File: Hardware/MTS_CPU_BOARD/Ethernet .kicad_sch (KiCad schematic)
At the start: 7 parts, among them J2 THD-02-R, U4 TPD4EUSB30, U5 TPD4EUSB30, U6 MagJack-A70-112-331N126

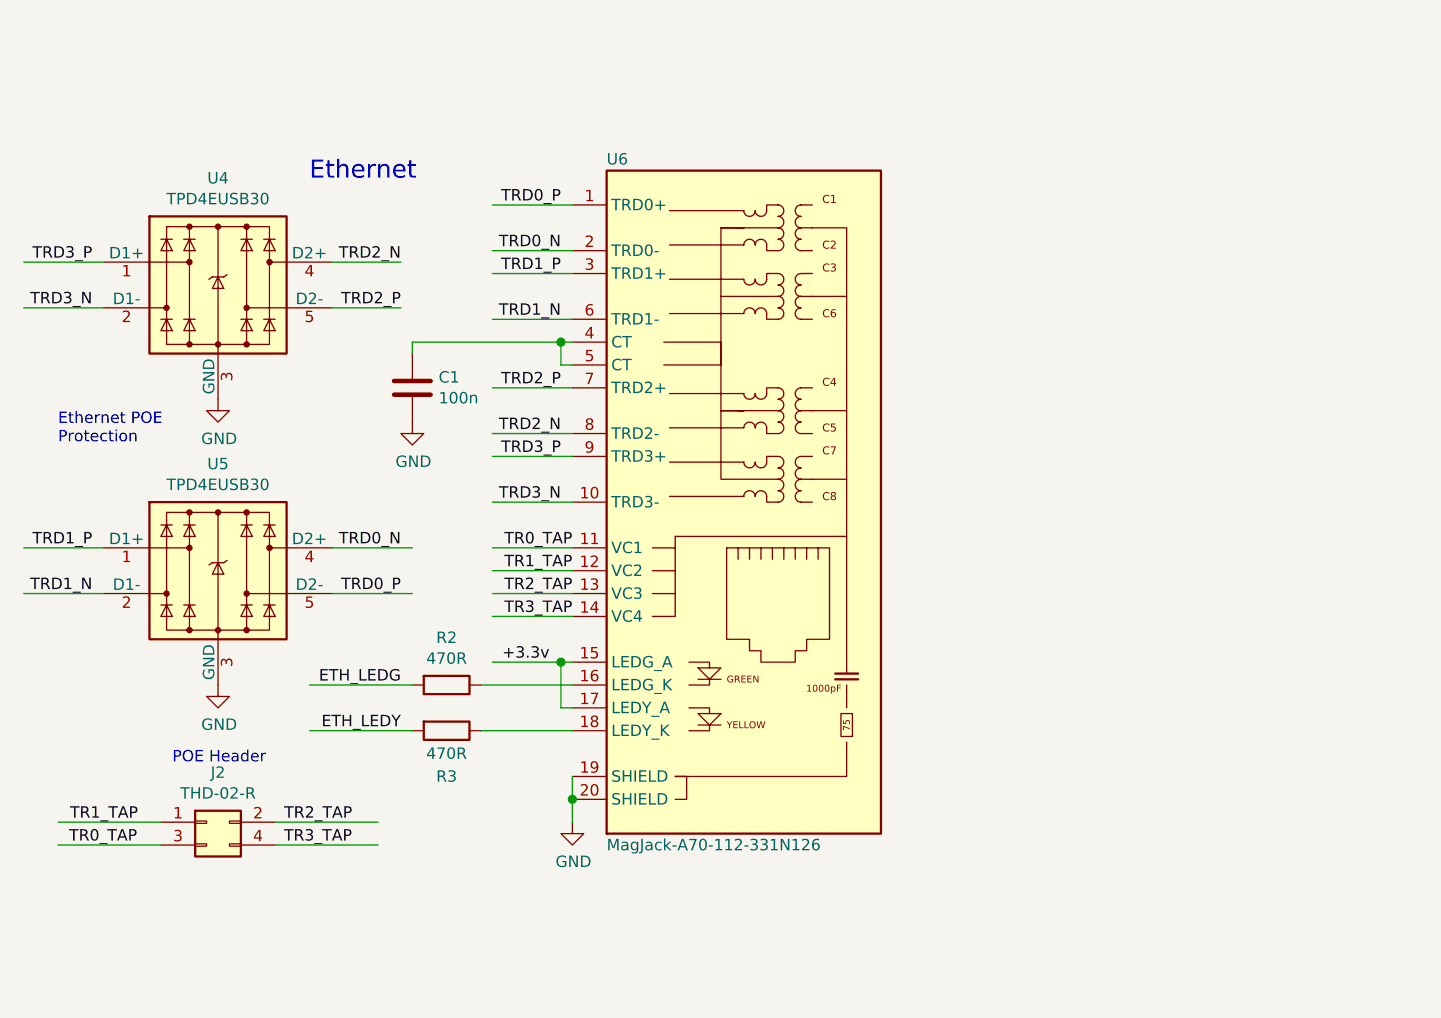
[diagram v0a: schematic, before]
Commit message: Add EtherCAT
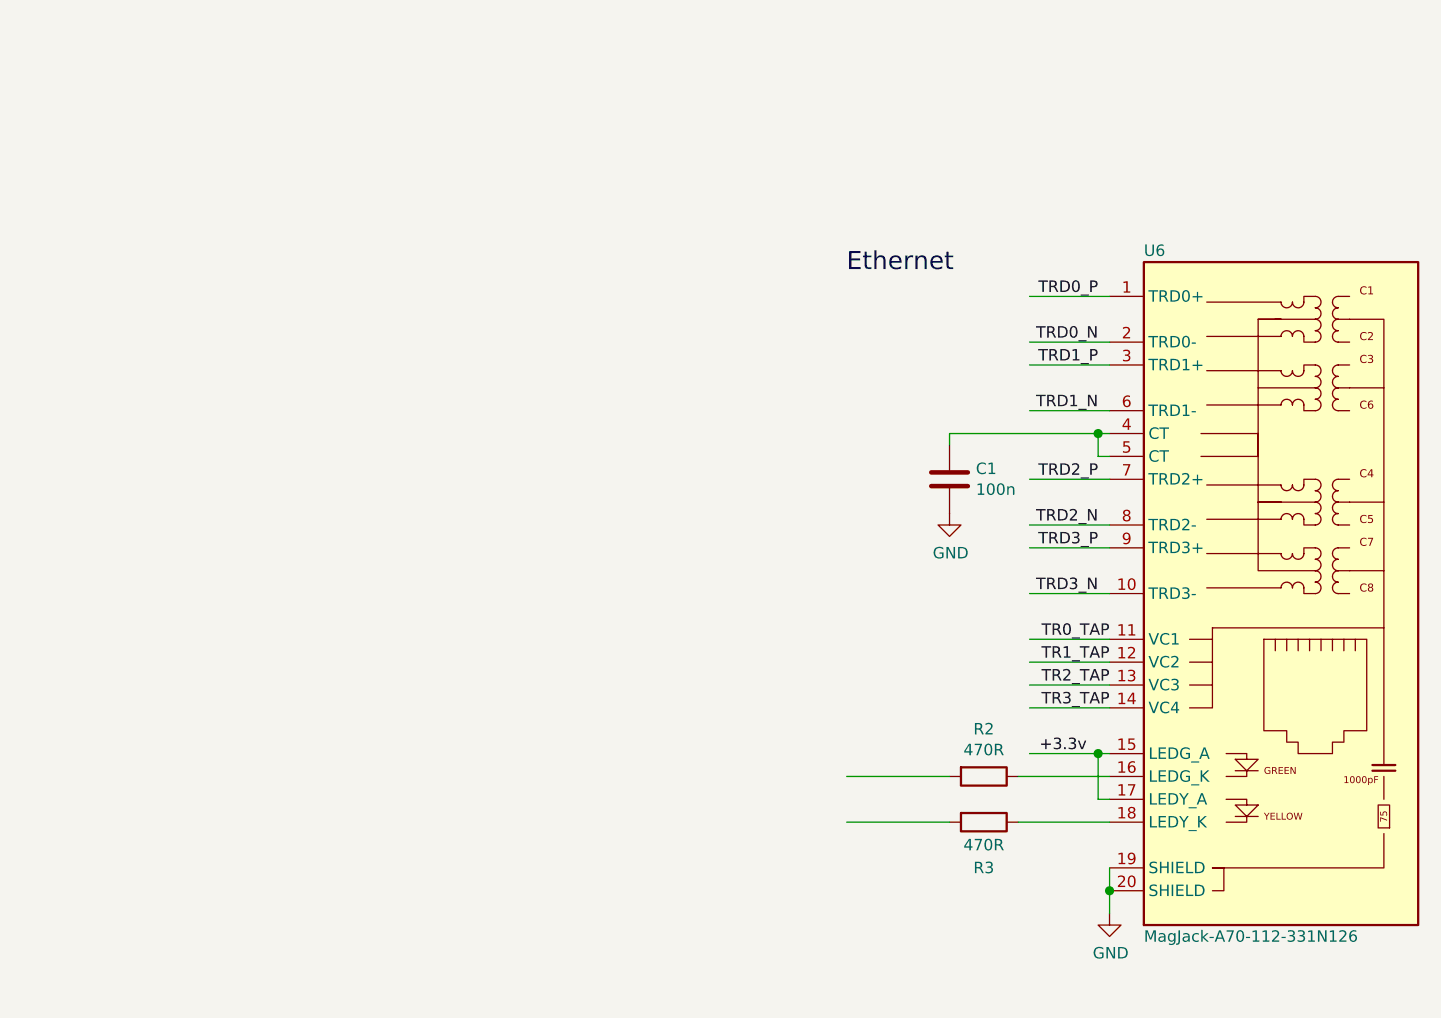
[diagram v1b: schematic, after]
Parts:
- removed J2: THD-02-R, Connector_PinHeader_2.54mm:PinHeader_2x02_P2.54mm_Vertical, symbol Connector_Generic:Conn_02x02_Odd_Even
- removed U4, U5: TPD4EUSB30, Package_SON:USON-10_2.5x1.0mm_P0.5mm, symbol CM4IO:TPD4EUSB30
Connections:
- net ETH_LEDG: no longer names the net of R2.2
- net ETH_LEDY: no longer names the net of R3.2
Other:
- note removed: "Ethernet POE Protection"
- note removed: "POE Header"
- moved on the sheet: C1, R2, R3, U6

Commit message: Add status Led´s
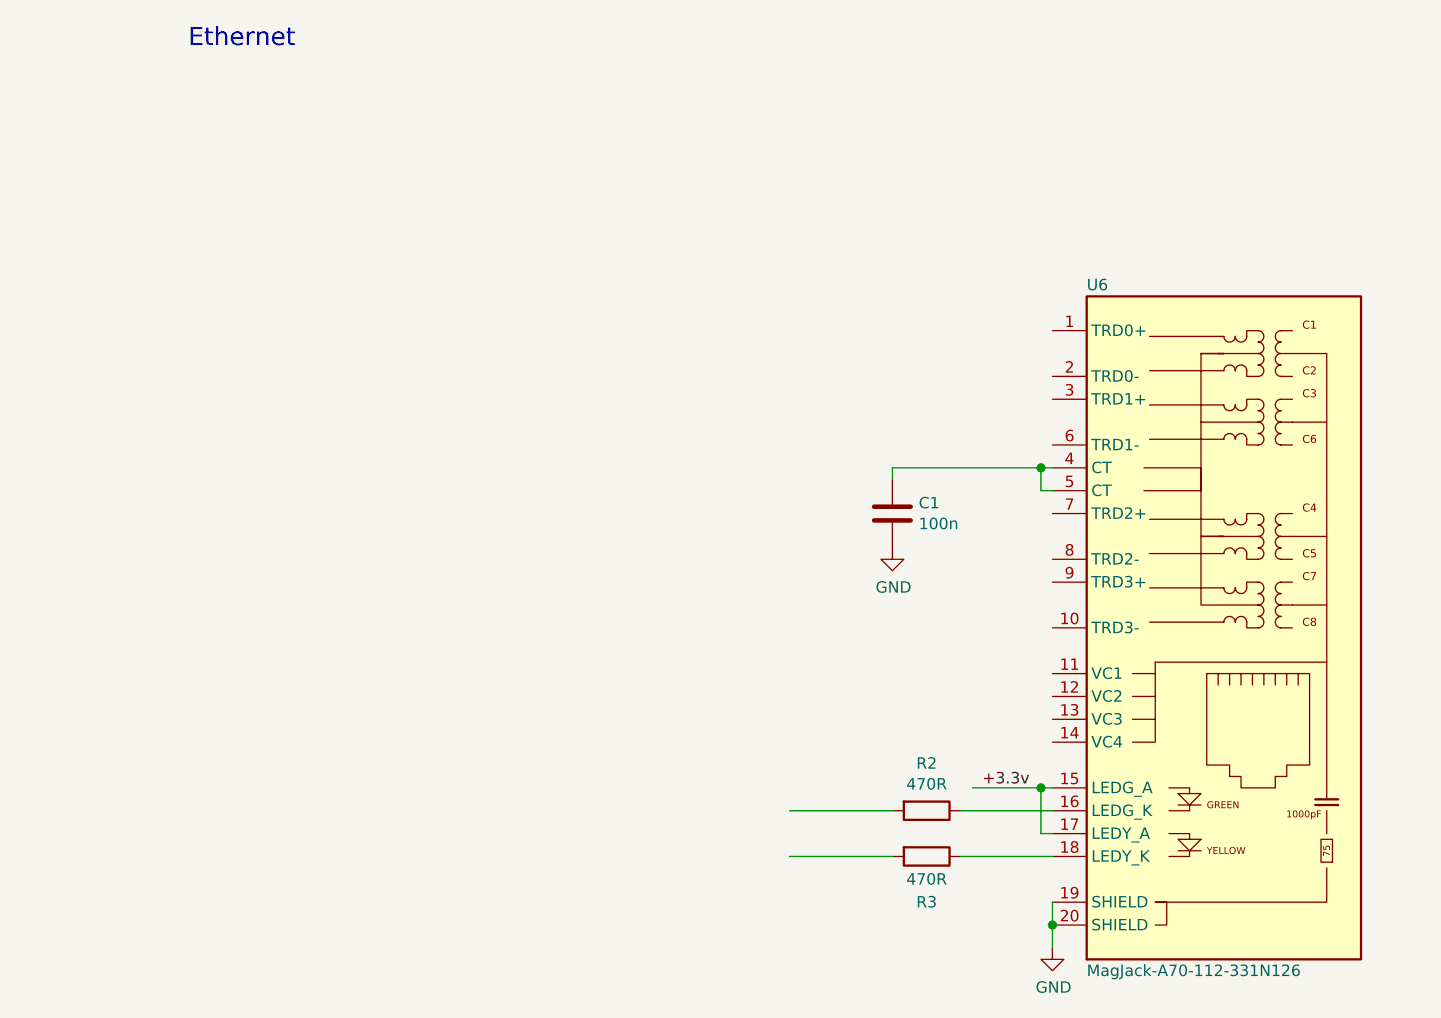
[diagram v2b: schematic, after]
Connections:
- net TR0_TAP: no longer names the net of U6.11 (VC1)
- net TR1_TAP: no longer names the net of U6.12 (VC2)
- net TR2_TAP: no longer names the net of U6.13 (VC3)
- net TR3_TAP: no longer names the net of U6.14 (VC4)
- net TRD0_N: no longer names the net of U6.2 (TRD0-)
- net TRD0_P: no longer names the net of U6.1 (TRD0+)
- net TRD1_N: no longer names the net of U6.6 (TRD1-)
- net TRD1_P: no longer names the net of U6.3 (TRD1+)
- net TRD2_N: no longer names the net of U6.8 (TRD2-)
- net TRD2_P: no longer names the net of U6.7 (TRD2+)
- net TRD3_N: no longer names the net of U6.10 (TRD3-)
- net TRD3_P: no longer names the net of U6.9 (TRD3+)
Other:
- moved on the sheet: C1, R2, R3, U6
